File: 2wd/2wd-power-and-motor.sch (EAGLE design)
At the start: 10 parts, among them J2 To Motherboard, J3 Right Motor, J4 Left Motor

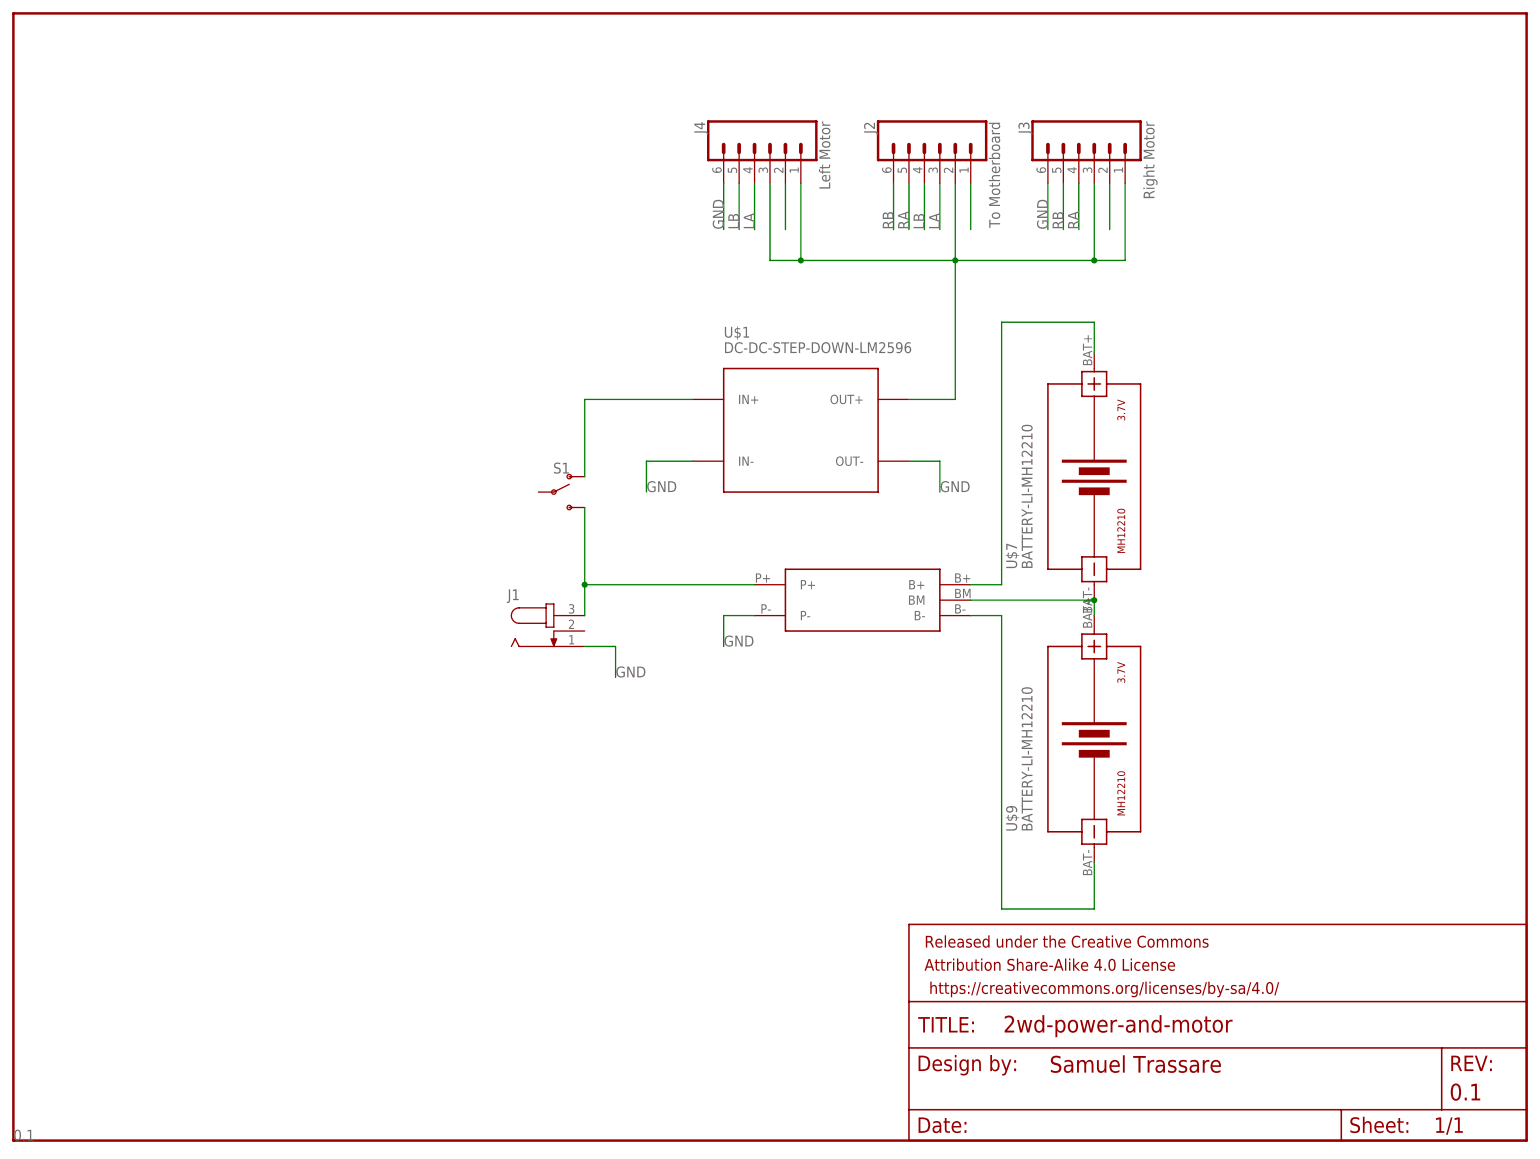
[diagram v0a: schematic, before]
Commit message: Resized board, added motor driver.
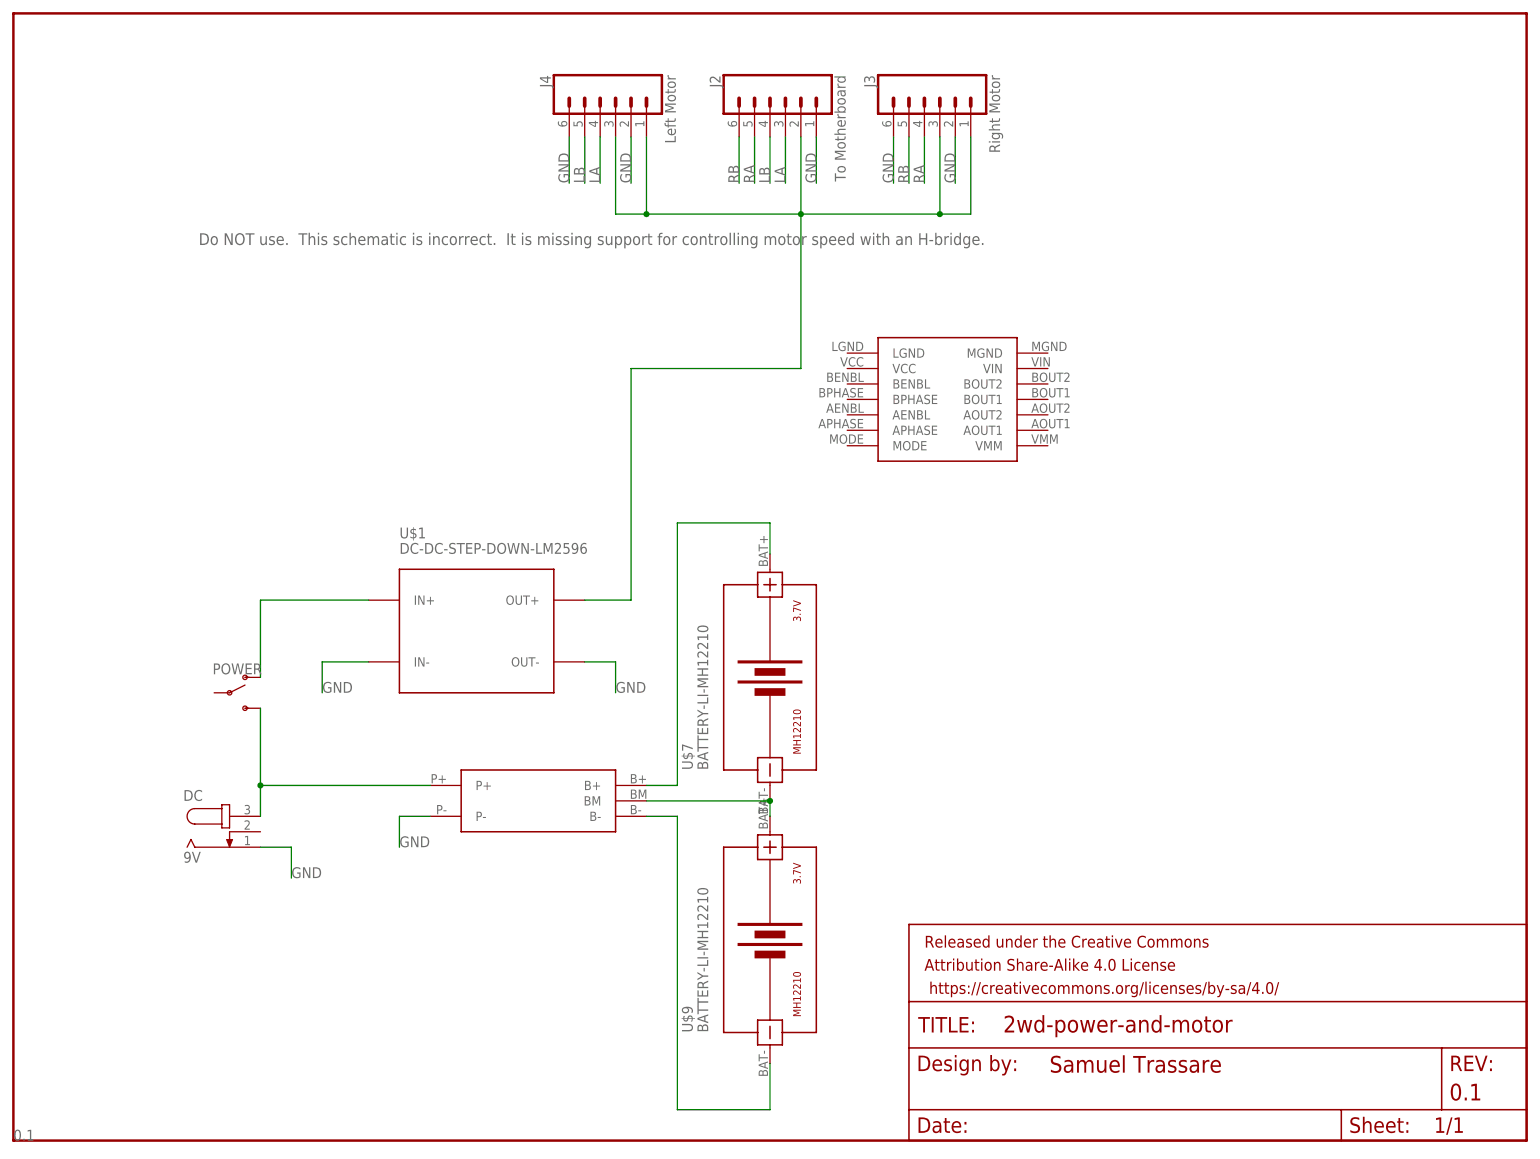
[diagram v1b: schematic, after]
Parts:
- removed J1: (no value), con-jack:JACK-PLUG0
- removed S1: (no value), SparkFun-Switches:SWITCH-SPDT-PTH-11.6X4.0MM
- added DC: 9V, con-jack:JACK-PLUG0
- added POWER: (no value), SparkFun-Switches:SWITCH-SPDT-PTH-11.6X4.0MM
- added U$2: POLOLU_MOTOR_DRV8835THROUGHHOLE, pololu:POLOLU_MOTOR_DRV8835THROUGHHOLE
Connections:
- net GND: now also DC.1; no longer J1.1
- net N$1: now also POWER.O; no longer S1.O
- net N$3: now also DC.3, POWER.S; no longer J1.3, S1.S
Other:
- note added: "Do NOT use. This schematic is incorrect. It is missing support for controlling motor speed with an H-bridge."
- moved on the sheet: J2, J3, J4, U$1, U$7, U$9

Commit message: Added integrated voltage regulation
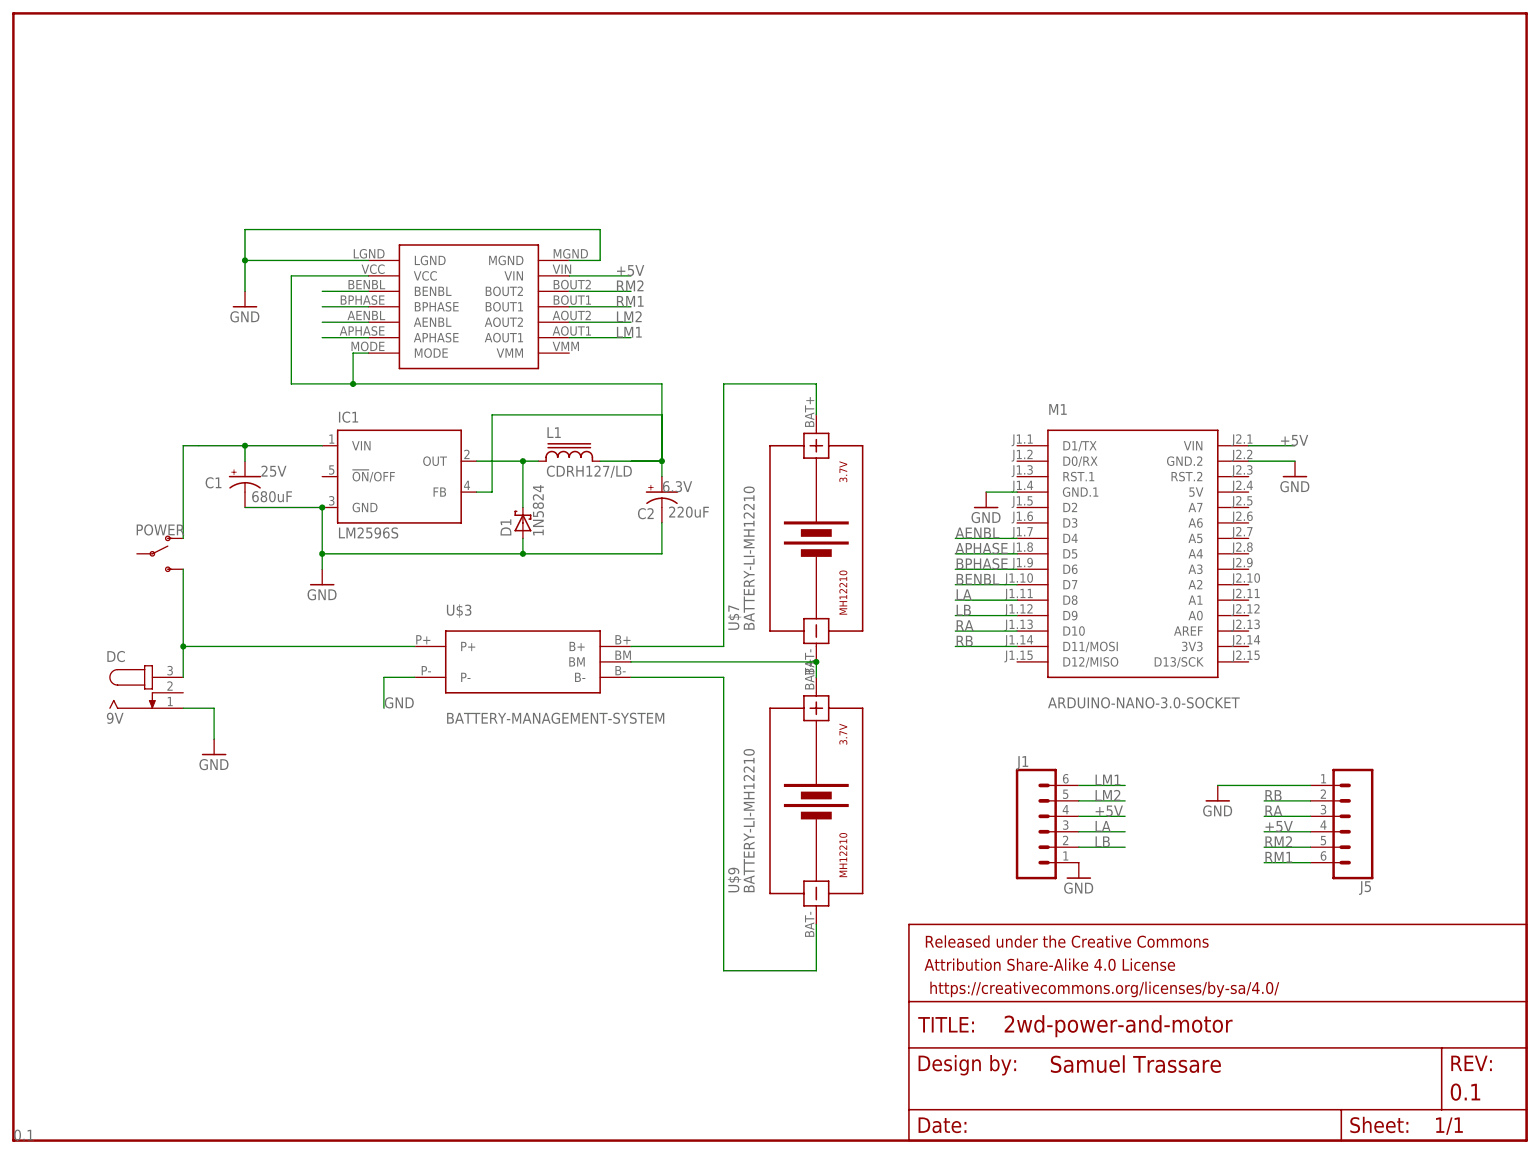
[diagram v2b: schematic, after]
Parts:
- removed 7V4-BMS: BMS, tiogaplanet:BMS
- removed J2: To Motherboard, SparkFun-Connectors:CONN_06NO_SILK_FEMALE_PTH
- removed J3: Right Motor, SparkFun-Connectors:CONN_06NO_SILK_FEMALE_PTH
- removed J4: Left Motor, SparkFun-Connectors:CONN_06NO_SILK_FEMALE_PTH
- removed U$1: DC-DC-STEP-DOWN-LM2596, diy-modules:DC-DC-STEP-DOWN-LM2596
- added C1: 680uF, rcl:CPOL-USE5-10.5
- added C2: 220uF, rcl:CPOL-USUD-6,3X5,8
- added D1: 1N5824, diode:SCHOTTKY-DIODESMD
- added IC1: LM2596S, national-semiconductor:LM2596S
- added J1: (no value), tiogaplanet:CONN_06LEFT_MOTOR_CONN
- added J5: (no value), tiogaplanet:CONN_06RIGHT_MOTOR_CONN
- added L1: CDRH127/LD, inductor-sumida:CDRH127/LD
- added M1: ARDUINO-NANO-3.0-SOCKET, tiogaplanet:ARDUINO-NANO-3.0-SOCKET
- added U$3: BATTERY-MANAGEMENT-SYSTEM, tiogaplanet:BATTERY-MANAGEMENT-SYSTEM
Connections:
- removed net N$2: J2.2, J3.1, J3.3, J4.1, J4.3, U$1.OUT+
- new net +5V: J1.4, J5.4, M1.VIN, U$2.VIN
- new net AENBL: M1.D4, U$2.AENBL
- new net APHASE: M1.D5, U$2.APHASE
- new net BENBL: M1.D7, U$2.BENBL
- new net BPHASE: M1.D6, U$2.BPHASE
- new net FB: C2.+, IC1.FB, L1.2
- new net LM1: J1.6, U$2.AOUT1
- new net LM2: J1.5, U$2.AOUT2
- new net N$10: U$2.MODE, U$2.VCC
- new net OUT: D1.C, IC1.OUT, L1.1
- new net RM1: J5.6, U$2.BOUT1
- new net RM2: J5.5, U$2.BOUT2
- new net VIN1: C1.+, IC1.VIN
- net GND: now also C1.-, C2.-, D1.A, IC1.GND, J1.1, J5.1, M1.GND.1, M1.GND.2, U$2.LGND, U$2.MGND, U$3.P-; no longer 7V4-BMS.P-, J2.1, J3.2, J3.6, J4.2, J4.6, U$1.IN-, U$1.OUT-
- net LA: now also J1.3, M1.D8; no longer J2.3, J4.4
- net LB: now also J1.2, M1.D9; no longer J2.4, J4.5
- net N$1: no longer U$1.IN+
- net N$3: now also U$3.P+; no longer 7V4-BMS.P+
- net N$4: now also U$3.B+; no longer 7V4-BMS.B+
- net N$5: now also U$3.B-; no longer 7V4-BMS.B-
- net N$6: now also U$3.BM; no longer 7V4-BMS.BM
- net RA: now also J5.3, M1.D10; no longer J2.5, J3.4
- net RB: now also J5.2, M1.D11/MOSI; no longer J2.6, J3.5
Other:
- note removed: "Do NOT use. This schematic is incorrect. It is missing support for controlling motor speed with an H-bridge."
- moved on the sheet: DC, POWER, U$7, U$9
